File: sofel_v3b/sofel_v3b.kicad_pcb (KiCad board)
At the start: 2 copper layers, 145.4 x 116.3 mm, 110 parts, among them J1 Pimaroni Trackball, J2 4PIN, J3 OLED, SW1 SW_PUSH_LED, SW10 SW_PUSH_LED, SW11 SW_PUSH_LED, SW12 SW_PUSH_LED, SW13 SW_PUSH_LED, SW14 SW_PUSH_LED, SW15 SW_PUSH_LED, SW16 SW_PUSH_LED, SW17 SW_PUSH_LED, SW18 SW_PUSH_LED, SW19 SW_PUSH_LED, SW2 SW_PUSH_LED, SW20 SW_PUSH_LED, SW21 SW_PUSH_LED, SW22 SW_PUSH_LED, SW23 SW_PUSH_LED, SW24 SW_PUSH_LED, SW25 Rotary_Encoder_Switch, SW26 SW_PUSH_LED, SW27 SW_PUSH_LED, SW28 SW_PUSH_LED, SW29 SW_PUSH_LED, SW3 SW_PUSH_LED, SW30 SW_PUSH_LED, SW4 SW_PUSH_LED, SW5 SW_PUSH_LED, SW6 SW_PUSH_LED, SW7 SW_PUSH_LED, SW8 SW_PUSH_LED, SW9 SW_PUSH_LED, U2 SN74AHCT1G125, U3 Pico

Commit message: Updated notes
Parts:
- removed the J1 at (86.7, 105.8)
- removed the J1 at (89.3, 105.8)
- removed the J1 at (84.2, 105.8)
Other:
- board text added: "Todo: Validate that the first sk6812 acts as a level shifter, then remove the level shifter bypass. WAIT: Consider removing volt shifter. Really hard to solder, may not be necessary. (Testing shifter bypass to asses SK6812 instead of SK6803) Lessons learned/TODO 5-22-23: WAIT: Remove OLED pin markings after prototype validation WAIT: The 4 holes in the keyplate need to be smaller, otherwise the p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"
- board text added: "v3.02->3.03: Improvements made while building prototype 3.02, included in version3.03 OLEDs incorrectly wired. GP6 went to SCL, and GP7 went to SDA, when those two should have been swtiched. Fixed, OLED jack moved -y 2.54*1.5 for visual balance. Pico footprint made holes wider and moved bottom hole down Pico flipped footprint so now pico jack faces board. Pico - fixed rectangular gnd pads (now sq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"
- board text removed: "Todo: Validate that the first sk6812 acts as a level shifter, then remove the level shifter bypass. WAIT: Consider removing volt shifter. Really hard to solder, may not be necessary. (Testing shifter bypass to asses SK6812 instead of SK6803) Lessons learned/TODO 5-22-23: Soleniod jack is at a dumb spot. it sticks out either way. tuck it up under so you can use dupont connectors. WAIT: Remove OLED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"
- board text removed: "v3.02->3.03: Improvements made while building prototype 3.02, included in version3.03 OLEDs incorrectly wired. GP6 went to SCL, and GP7 went to SDA, when those two should have been swtiched. Instead of unswitching, I moved the OLED to GP27(SCL) and GP 26(SDA). Firmware needs to be updated for this change. The new pins still use I2C1 instead of I2C0, so that does not need to be updated. OLED jack 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"

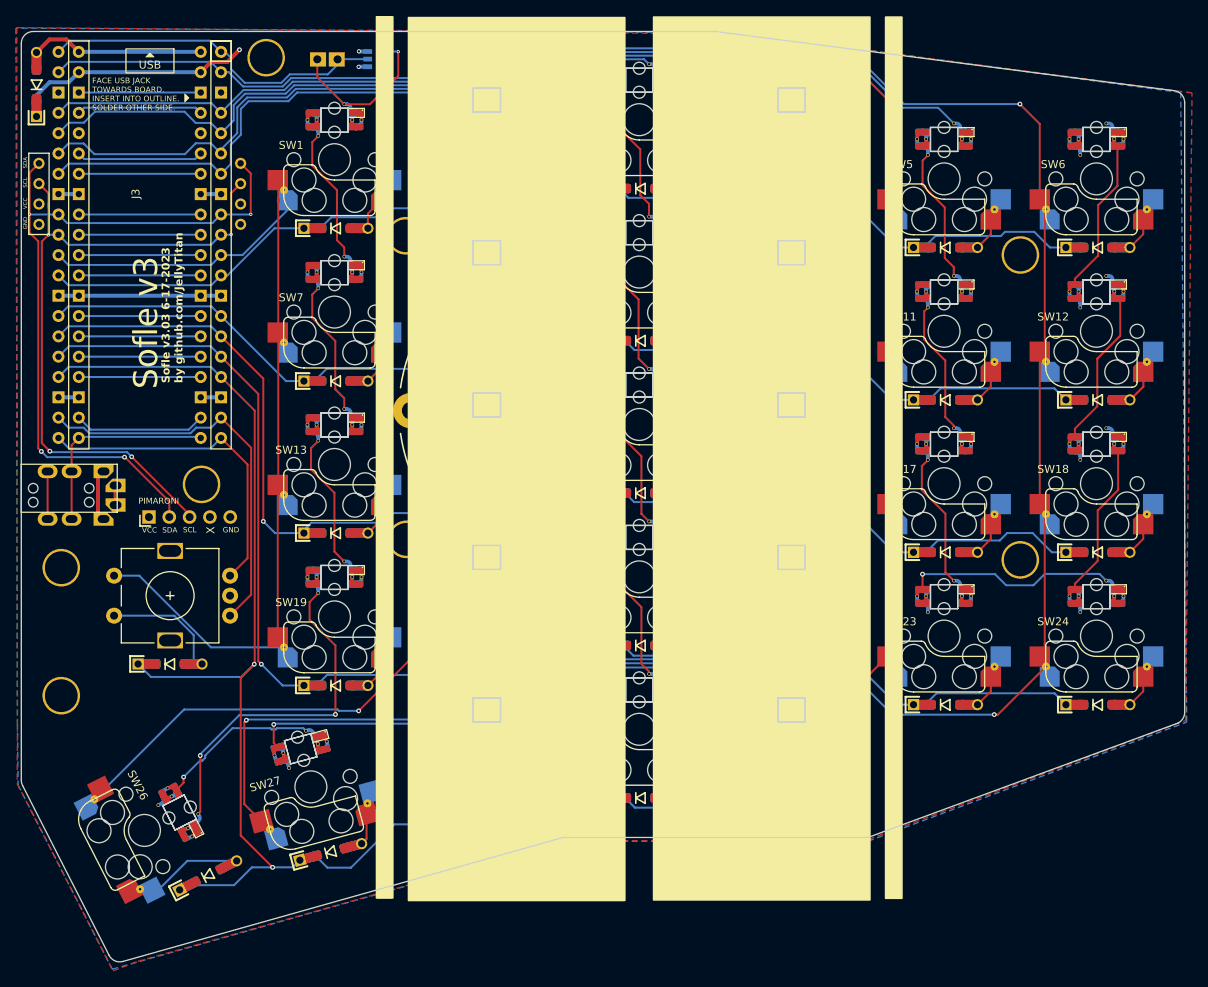
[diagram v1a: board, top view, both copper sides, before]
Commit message: Improved led gnd markings reduced led tweezer hole size added markings for key plate post holes moved pimornoi traces
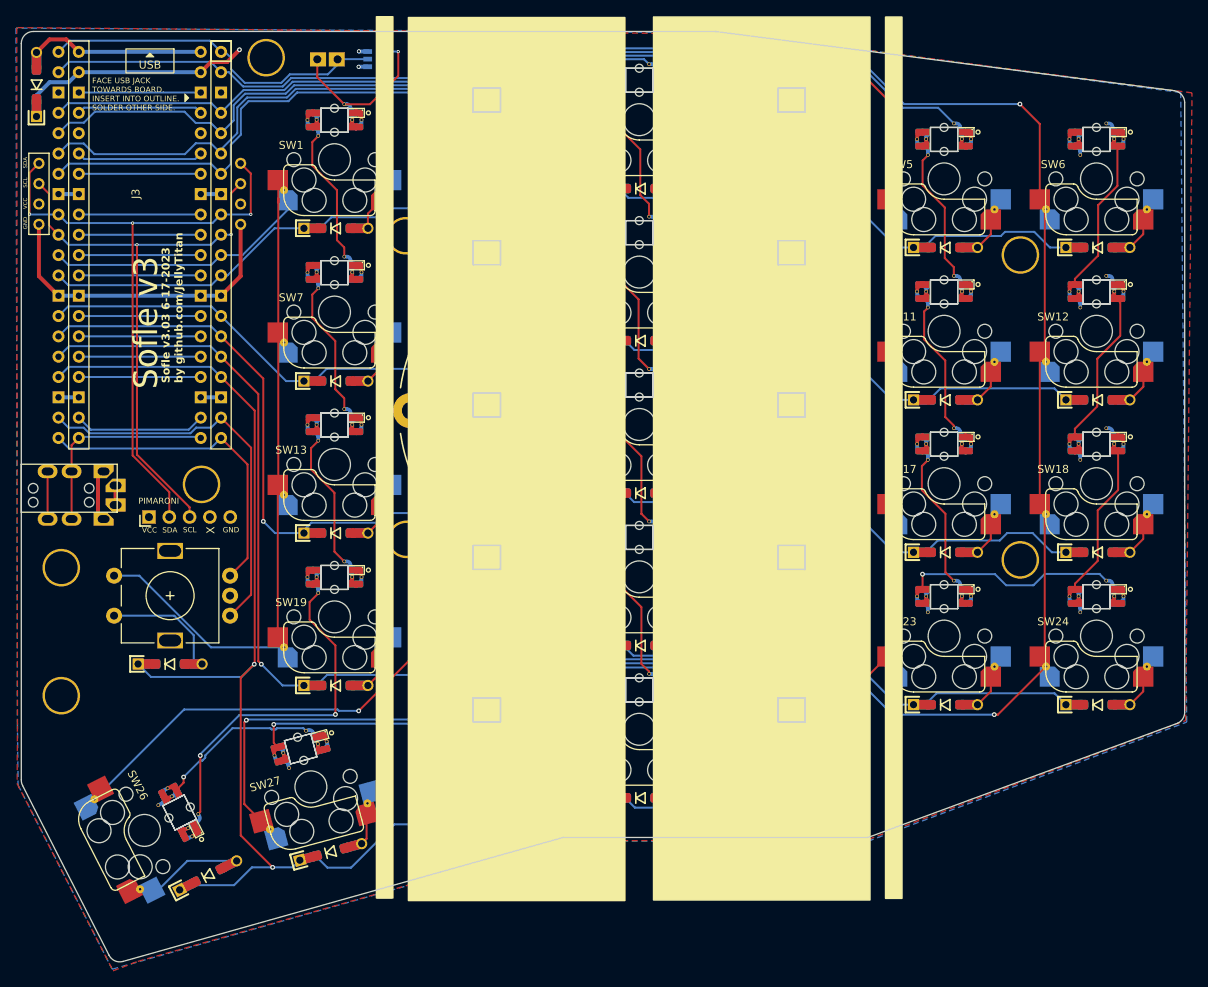
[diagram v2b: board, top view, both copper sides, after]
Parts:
- SW1, SW10, SW11, SW12, SW13, SW14, SW15, SW16, SW17, SW18, SW19, SW2, SW20, SW21, SW22, SW23, SW24, SW26, SW27, SW28, SW29, SW3, SW30, SW4, SW5, SW6, SW7, SW8, SW9: footprint sofle_v3b:Cherry_MX_DS_Hotswap_miniE_1U -> sofle_v3b:Cherry_MX_DS_Hotswap_miniE_1U_v3.03
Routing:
- net GND: track 35.4 -> 55.3 mm
- net SCL: track 87.0 -> 73.6 mm, vias 4 -> 2
- net SDA: track 93.1 -> 81.0 mm, vias 4 -> 3
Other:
- board text added: "v3.02->3.03: Improvements made while building prototype 3.02, included in version3.03 OLEDs incorrectly wired. GP6 went to SCL, and GP7 went to SDA, when those two should have been swtiched. Fixed, OLED jack moved -y 2.54*1.5 for visual balance. Pico footprint made through-holes for buttons wider and moved bottom hole down Added extra marking for LED grounds. (OUtline marking was obscured by pad)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"
- board text removed: "v3.02->3.03: Improvements made while building prototype 3.02, included in version3.03 OLEDs incorrectly wired. GP6 went to SCL, and GP7 went to SDA, when those two should have been swtiched. Fixed, OLED jack moved -y 2.54*1.5 for visual balance. Pico footprint made holes wider and moved bottom hole down Pico flipped footprint so now pico jack faces board. Pico - fixed rectangular gnd pads (now sq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"

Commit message: Added keyplate layer Added keyplate and backplate .step
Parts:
- TH1: footprint SofleChocLoud:Hole from sofle for M2 posts gold rimmer -> sofle_v3b:Hole from sofle for M2 posts gold rimmer
